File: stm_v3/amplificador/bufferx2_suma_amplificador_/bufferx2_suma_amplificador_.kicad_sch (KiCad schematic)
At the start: 142 parts, among them J1 ADS1115, J10 MCP4725_2C, J11 MCP4725_2F, J12 MCP4725_3C, J13 MCP4725_3F, J14 MCP4725_4C, J15 MCP4725_4F, J16 MCP4725_1F, J17 Screw_Terminal_01x04, J18 Sample, J19 signal_in, J2 MCP4725_VBIAS, J20 Terminal_01x02, J3 FC03, J4 muxL_1-12, J5 muxR_13-24, J6 espL_1-19, J7 espR_20-38, J8 Driver_motor, J9 MCP4725_1C, Q1 2N3904, Q2 2N3906, Q3 2N3904, Q4 2N3906, Q5 2N3904, Q6 2N3906, Q7 2N3904, Q8 2N3906, SW1 E stop, SW2 Retraction, U1 PC817, U10 TL074, U2 PC817, U3 OPA124U, U4 TL074, U5 TL074, U6 TL074, U7 TL074, U8 TL071, U9 TL071

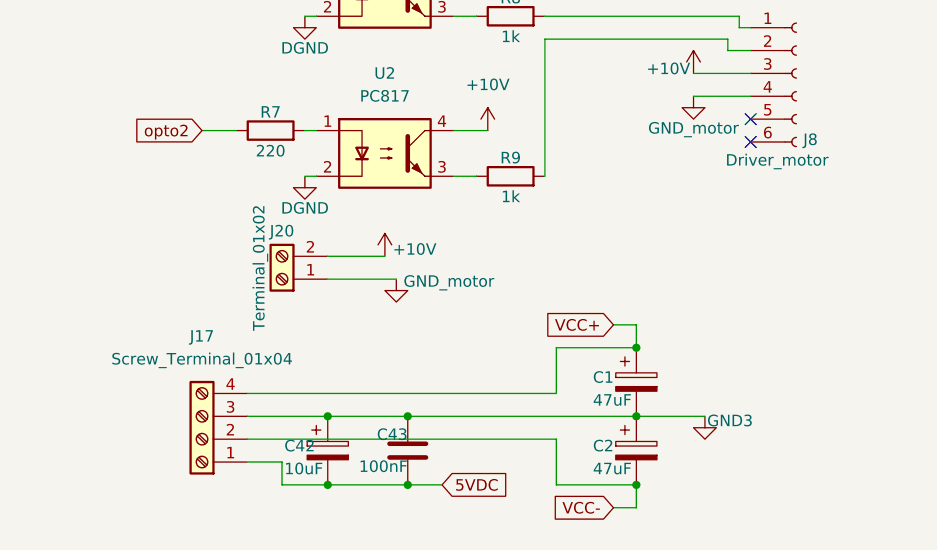
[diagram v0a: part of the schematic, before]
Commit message: finalizado STM y fuente de poder limpia, todo conforme a las huellas.
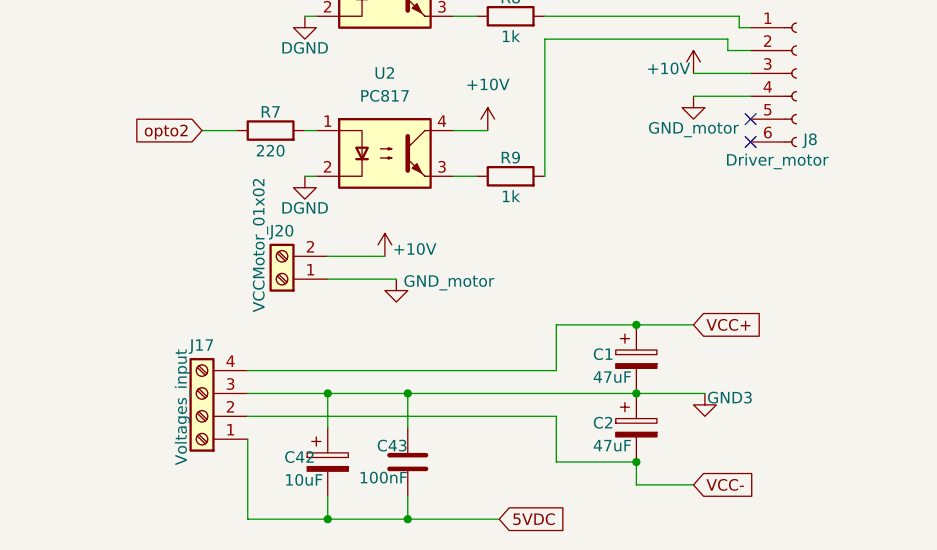
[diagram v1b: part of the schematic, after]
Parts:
- C31, C32, C33, C34, C35, C36, C37, C38: footprint Capacitor_THT:C_Disc_D5.0mm_W2.5mm_P2.50mm -> Capacitor_THT:C_Disc_D3.0mm_W1.6mm_P2.50mm
- C43: footprint (none) -> Capacitor_THT:C_Rect_L9.0mm_W3.6mm_P7.50mm_MKT
- J17: value Screw_Terminal_01x04 -> Voltages_input
- J20: value Terminal_01x02 -> VCCMotor_01x02
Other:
- moved on the sheet: C1, C2, C42, C43, J17
